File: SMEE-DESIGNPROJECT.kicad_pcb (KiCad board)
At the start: 2 copper layers, 25.5 x 110 mm, 15 parts, among them J1 Conn_02x03_Odd_Even, U2 LM555xN

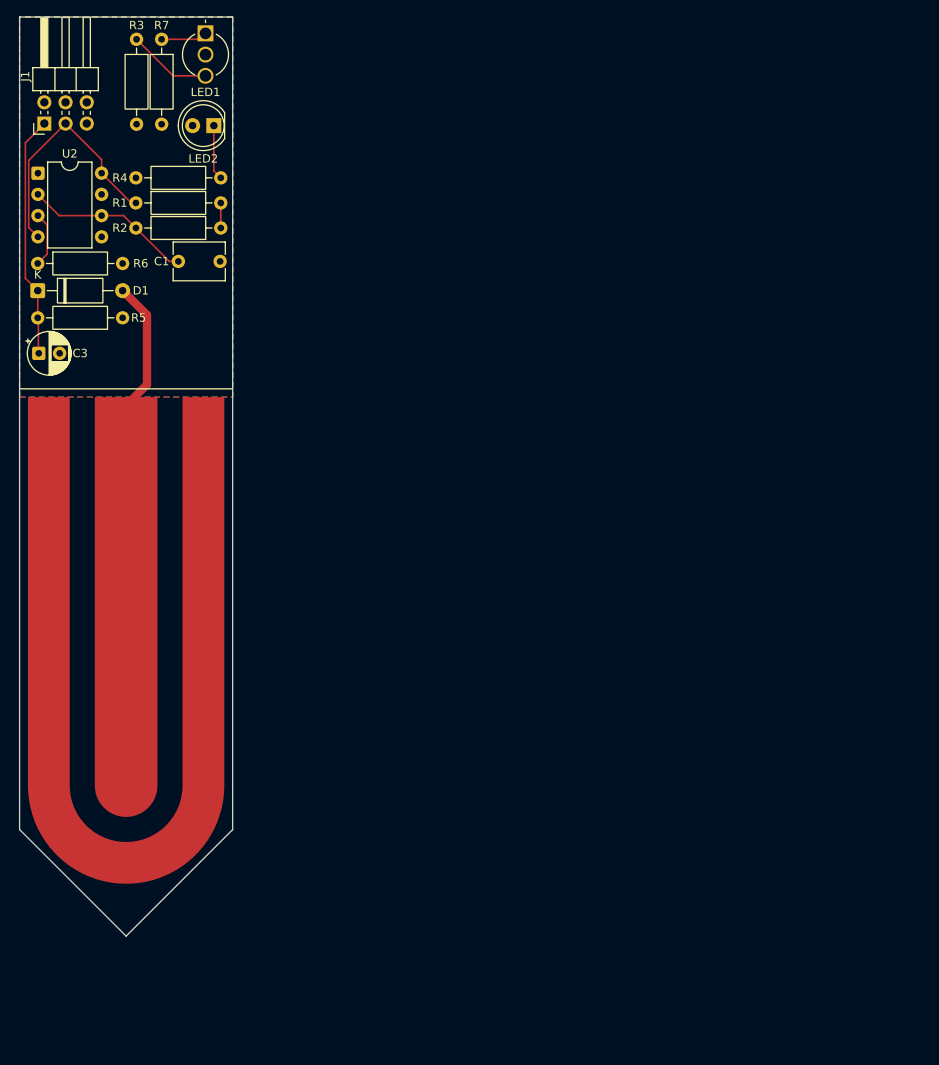
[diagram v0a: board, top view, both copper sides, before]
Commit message: Reposition PCB components; add title block & PDFs
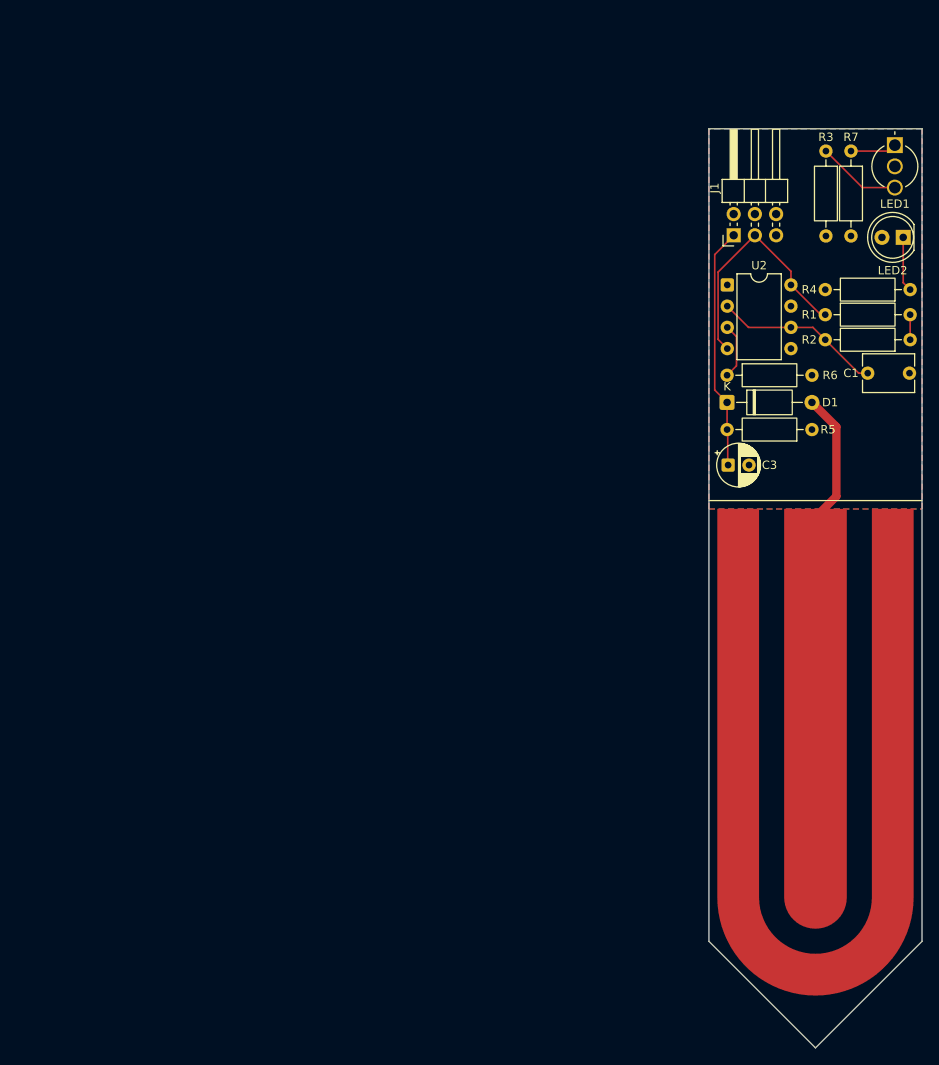
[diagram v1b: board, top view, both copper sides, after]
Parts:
- moved R2 83.6 mm to (140.1, 71.6)
- moved R4 83.6 mm to (140.1, 65.6)
- moved R5 83.6 mm to (128.3, 82.4)
- moved C1 83.6 mm to (135.0, 75.6)
- moved C2 83.6 mm to (131.5, 105.9)
- moved C3 83.6 mm to (118.3, 86.6)
- moved D1 83.6 mm to (118.2, 79.1)
- moved J1 83.6 mm to (119.0, 59.1)
- moved LED1 83.6 mm to (138.2, 48.3)
- moved LED2 83.6 mm to (139.2, 59.4)
- moved R3 83.6 mm to (130.0, 49.0)
- moved R6 83.6 mm to (118.2, 75.9)
- moved R7 83.6 mm to (133.0, 49.0)
- moved U2 83.6 mm to (118.2, 65.1)
- moved R1 83.6 mm to (129.9, 68.6)

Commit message: Updated unrouted traces
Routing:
- net Net-(U2-DIS): track 3.00 -> 19.3 mm
- net /LED_R: track 0.00 -> 13.5 mm
- net +3.3V: track 29.1 -> 42.1 mm
- net /LED_G: track 0.00 -> 8.41 mm
- net Net-(D1-A): track 16.0 -> 19.2 mm
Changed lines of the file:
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@@
+	)
+	(segment
+		(start 131.375 68.625)
+		(end 129.92 68.625)
+		(width 0.2)
+		(layer "F.Cu")
+		(net 1)
+	)
+	(segment
+		(start 136.71 59.375)
+		(end 136.71 63.29)
+		(width 0.2)
+		(layer "F.Cu")
+		(net 1)
 	)
 	(segment
@@
 	)
 	(segment
+		(start 136.71 63.29)
+		(end 131.375 68.625)
+		(width 0.2)
+		(layer "F.Cu")
+		(net 1)
+	)
+	(segment
 		(start 117.094 63.531)
 		(end 121.5 59.125)
@@
 	)
 	(segment
+		(start 128.33 75.875)
+		(end 128.33 79.125)
+		(width 1)
+		(layer "F.Cu")
+		(net 4)
+	)
+	(segment
 		(start 131.25 82.045)
 		(end 131.25 90.3625)
@@
 	)
 	(segment
+		(start 126.94637 67.605)
+		(end 129.86537 70.524)
+		(width 0.2)
+		(layer "F.Cu")
+		(net 6)
+	)
+	(segment
+		(start 129.86537 70.524)
+		(end 138.181 70.524)
+		(width 0.2)
+		(layer "F.Cu")
+		(net 6)
+	)
+	(segment
 		(start 140.08 71.625)
 		(end 140.08 68.625)
@@
 	)
 	(segment
+		(start 138.181 70.524)
+		(end 140.08 68.625)
+		(width 0.2)
+		(layer "F.Cu")
+		(net 6)
+	)
+	(segment
+		(start 125.815 67.605)
+		(end 126.94637 67.605)
+		(width 0.2)
+		(layer "F.Cu")
+		(net 6)
+	)
+	(segment
 		(start 119.296 71.246)
 		(end 118.195 70.145)
@@
 	)
 	(segment
+		(start 129.5 56.5)
+		(end 130 57)
+		(width 0.2)
+		(layer "F.Cu")
+		(net 9)
+	)
+	(segment
+		(start 124.125 56.5)
+		(end 129.5 56.5)
+		(width 0.2)
+		(layer "F.Cu")
+		(net 9)
+	)
+	(segment
+		(start 124.04 56.585)
+		(end 124.125 56.5)
+		(width 0.2)
+		(layer "F.Cu")
+		(net 9)
+	)
+	(segment
+		(start 130 57)
+		(end 130 59.205)
+		(width 0.2)
+		(layer "F.Cu")
+		(net 9)
+	)
+	(segment
+		(start 122.651 55.434)
+		(end 121.5 56.585)
+		(width 0.2)
+		(layer "F.Cu")
+		(net 10)
+	)
+	(segment
+		(start 129.229 55.434)
+		(end 122.651 55.434)
+		(width 0.2)
+		(layer "F.Cu")
+		(net 10)
+	)
+	(segment
+		(start 133 59.205)
+		(end 129.229 55.434)
+		(width 0.2)
+		(layer "F.Cu")
+		(net 10)
+	)
+	(segment

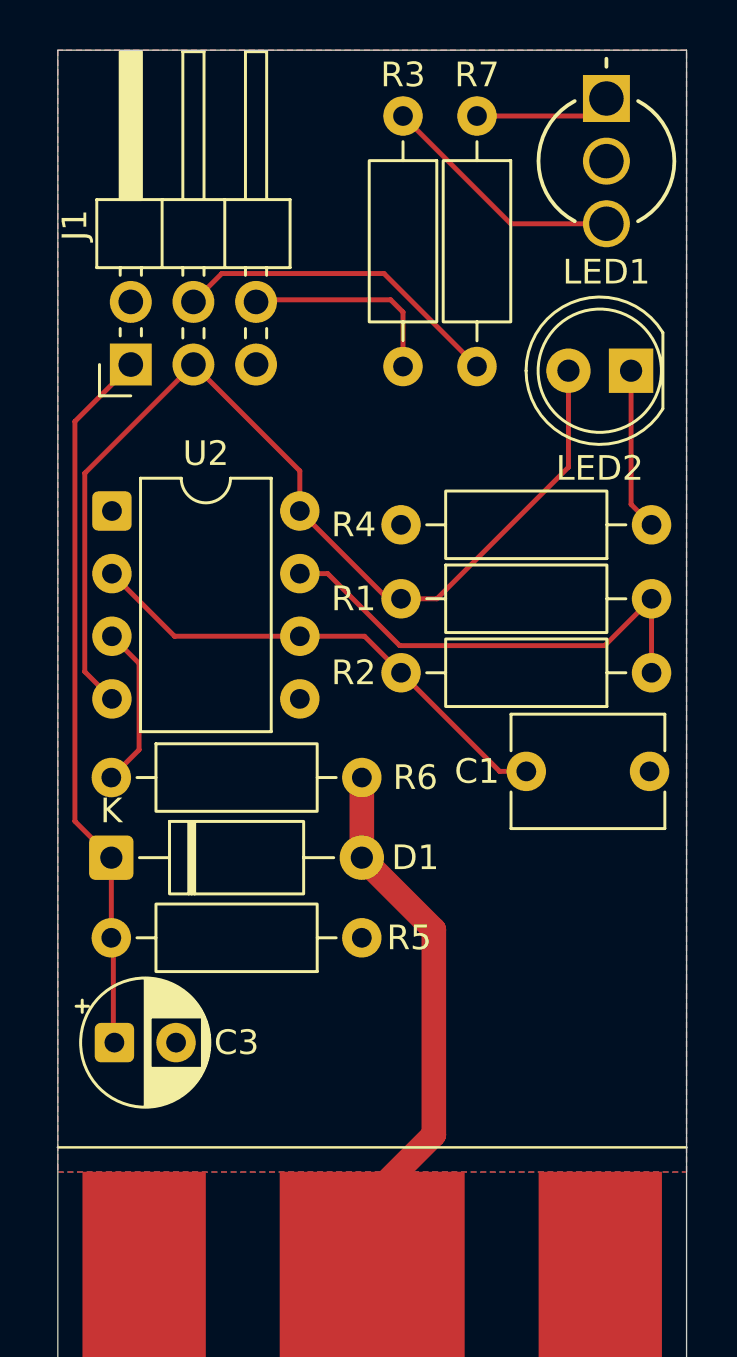
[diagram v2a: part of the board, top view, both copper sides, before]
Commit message: Enable teardrops and update PCB geometry
Add automatic backups and lock file; update KiCad project and PCB to enable teardrops on many pads/vias and adjust copper geometry. This change inserts teardrop settings for numerous pads, adds a teardrop zone ($teardrop_padvia$) with pad/via type and updated zone fill parameters, and updates many segment coordinates, widths and UUIDs to match the regenerated routing. Included three backup .zip files and a temporary .lck file.
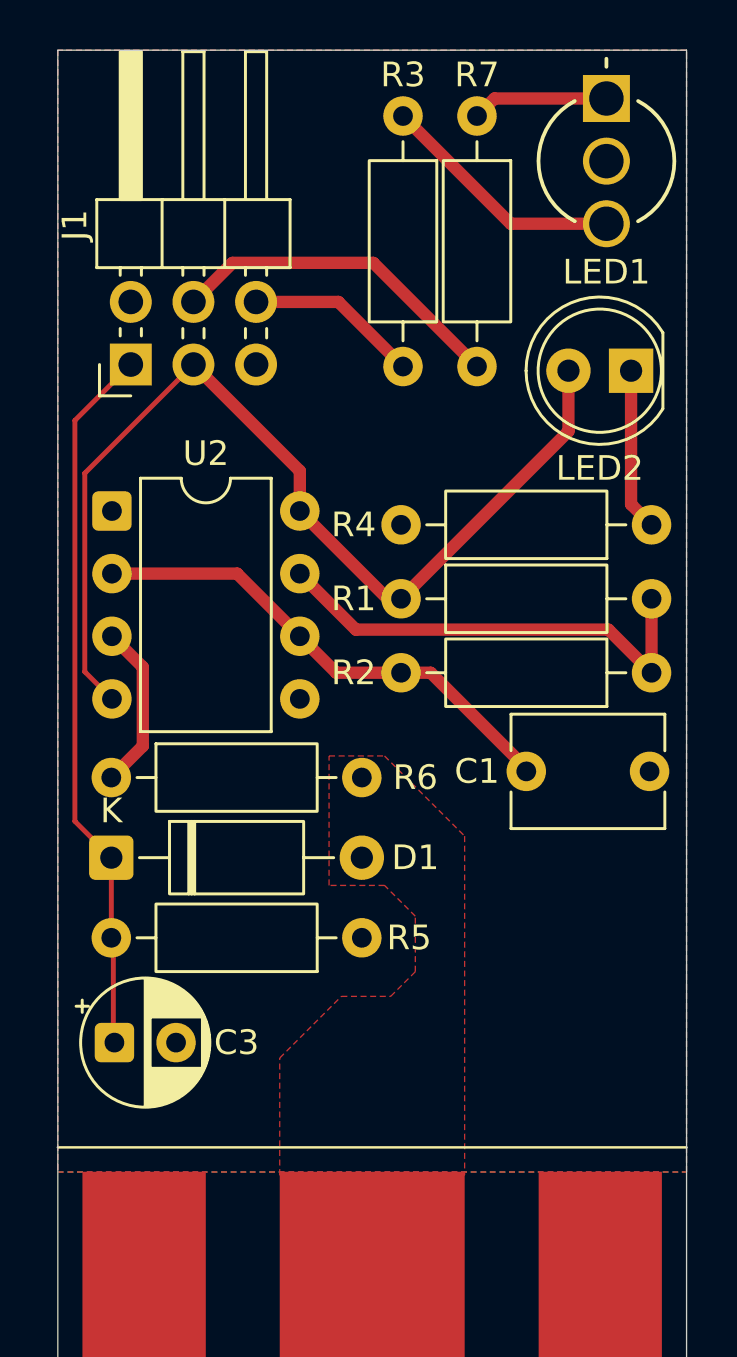
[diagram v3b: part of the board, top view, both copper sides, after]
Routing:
- net Net-(D1-A): track 19.2 -> 0.00 mm
- net /LED_G: track 8.41 -> 7.05 mm
- net +3.3V: track 42.1 -> 41.2 mm
- added copper zone on F.Cu, net Net-(D1-A)

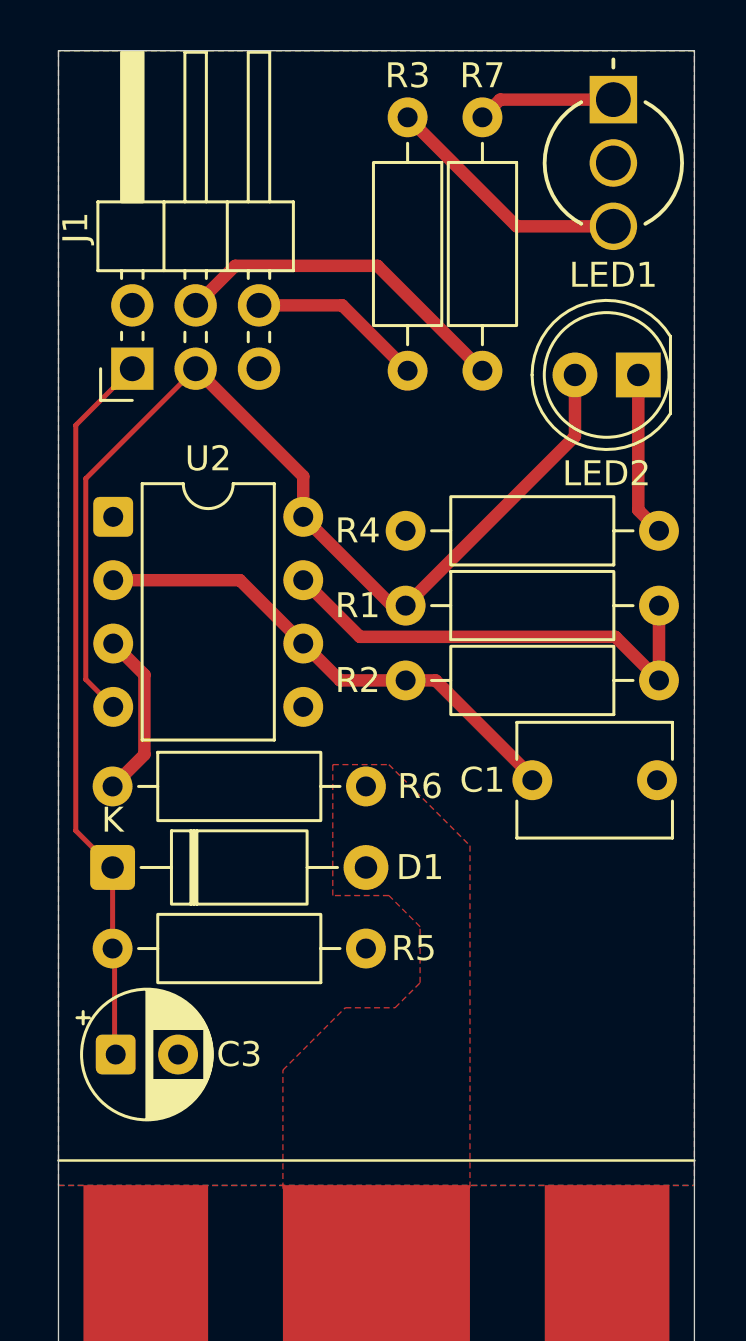
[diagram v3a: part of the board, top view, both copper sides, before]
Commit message: Update PCB layout and backups
Change component value (Value: 330 → 100) and perform extensive PCB layout edits: reroute segments, update zone polygons, net assignments, priorities, teardrop attributes, min_thickness/fill settings, island removal and many UUIDs for F.Cu features. Update related project (.kicad_prl) and schematic (.kicad_sch) files to match layout changes. File-level housekeeping: remove one old backup ZIP and add three new backup ZIP snapshots. These changes correct net/geometry assignments and tidy PCB fill/zone settings.
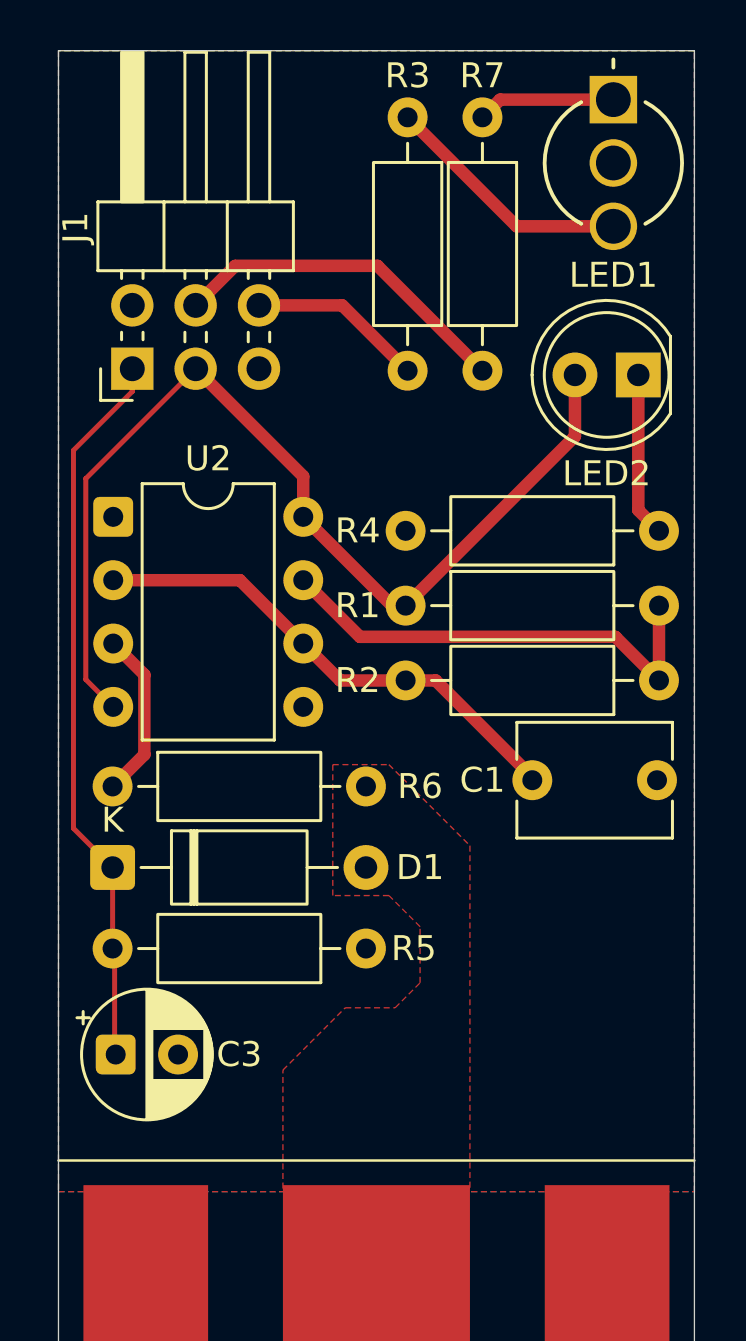
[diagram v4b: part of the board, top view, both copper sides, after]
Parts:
- R4: value 330 -> 100
